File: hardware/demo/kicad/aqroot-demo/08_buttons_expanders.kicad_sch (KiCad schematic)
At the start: 30 parts, among them SW2 A_SELECT, SW3 UP, SW4 DOWN, SW5 LEFT, SW6 RIGHT, SW7 B_BACK, U2 PCAL9535APW, U3 PCAL9535APW

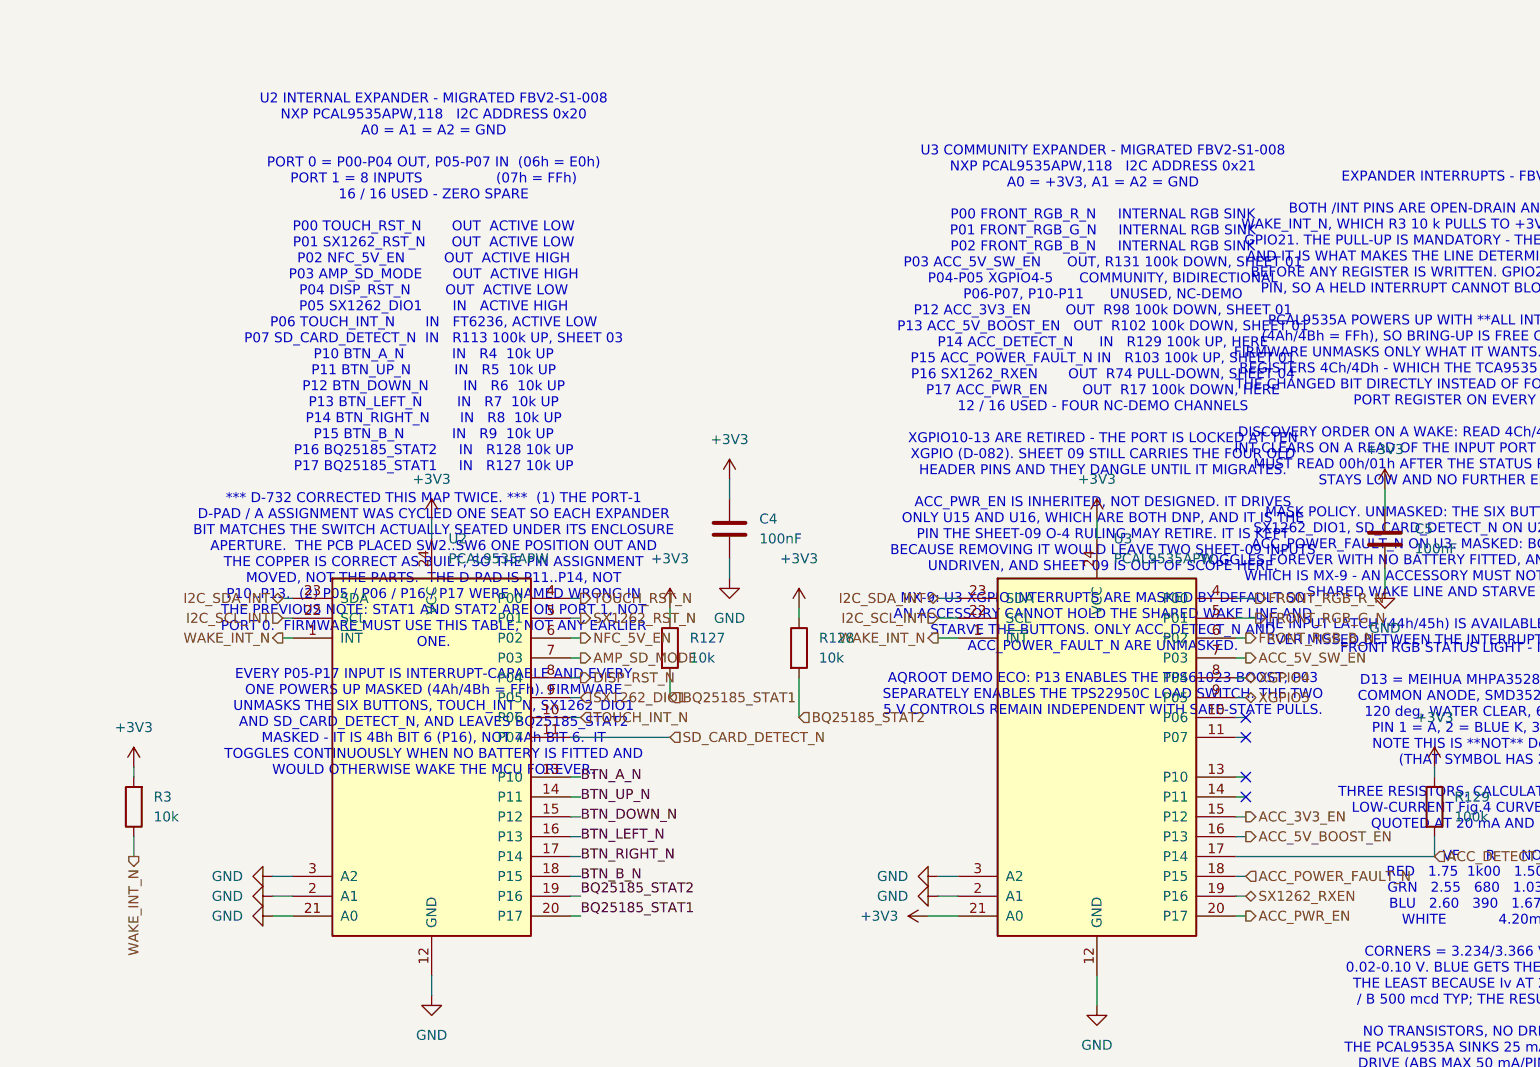
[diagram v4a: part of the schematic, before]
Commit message: demo: D-733 -- /ACC_PWR_EN is ROUTED and the community port's I2C buffer has its enable. 4 -> 3 retained open edges. What was holding it was /BQ25185_STAT1's 115.638 mm, 45-object western loop, which owns the only corridor from U16 into the U2-U3 pair; D-728 and D-731 both measured that ripping it closes ACC_PWR_EN and both stopped because STAT1 could not re-lay. D-732's lever opens it: an expander pin is a free variable, and STAT1's own surviving copper already passes 1.175 mm from U3.20 -- so STAT1 takes U3.20, ACC_PWR_EN takes the U2.20 that releases, and the loop is deleted. Both expanders are PCAL9535APW on the same internal bus sharing WAKE_INT_N, so the swap is behaviourally neutral; U2 P17 becomes that port's only output (07h FFh->7Fh) and R17's 100k keeps the safe state. STAT1's tail is a 1.025 mm hand lay that goes north first because U3's 1.475 mm lands make the straight 45-degree continuation pass 0.066 mm from U3.21. ACC_PWR_EN routes U16.1->U2.20 in 54.57 mm / 4 barrels, and only at 25 um: the 50 um rung is 0.47 mm shorter and carries a copper_sliver. Gate all clauses TRUE, verify_promotion PASS, DRC {lib_footprint_issues:199} only, parity 246/0 errors, 14/14 contracts PASS, protected_copper IDENTICAL.
Co-Authored-By: Claude Opus 5 <noreply@anthropic.com>
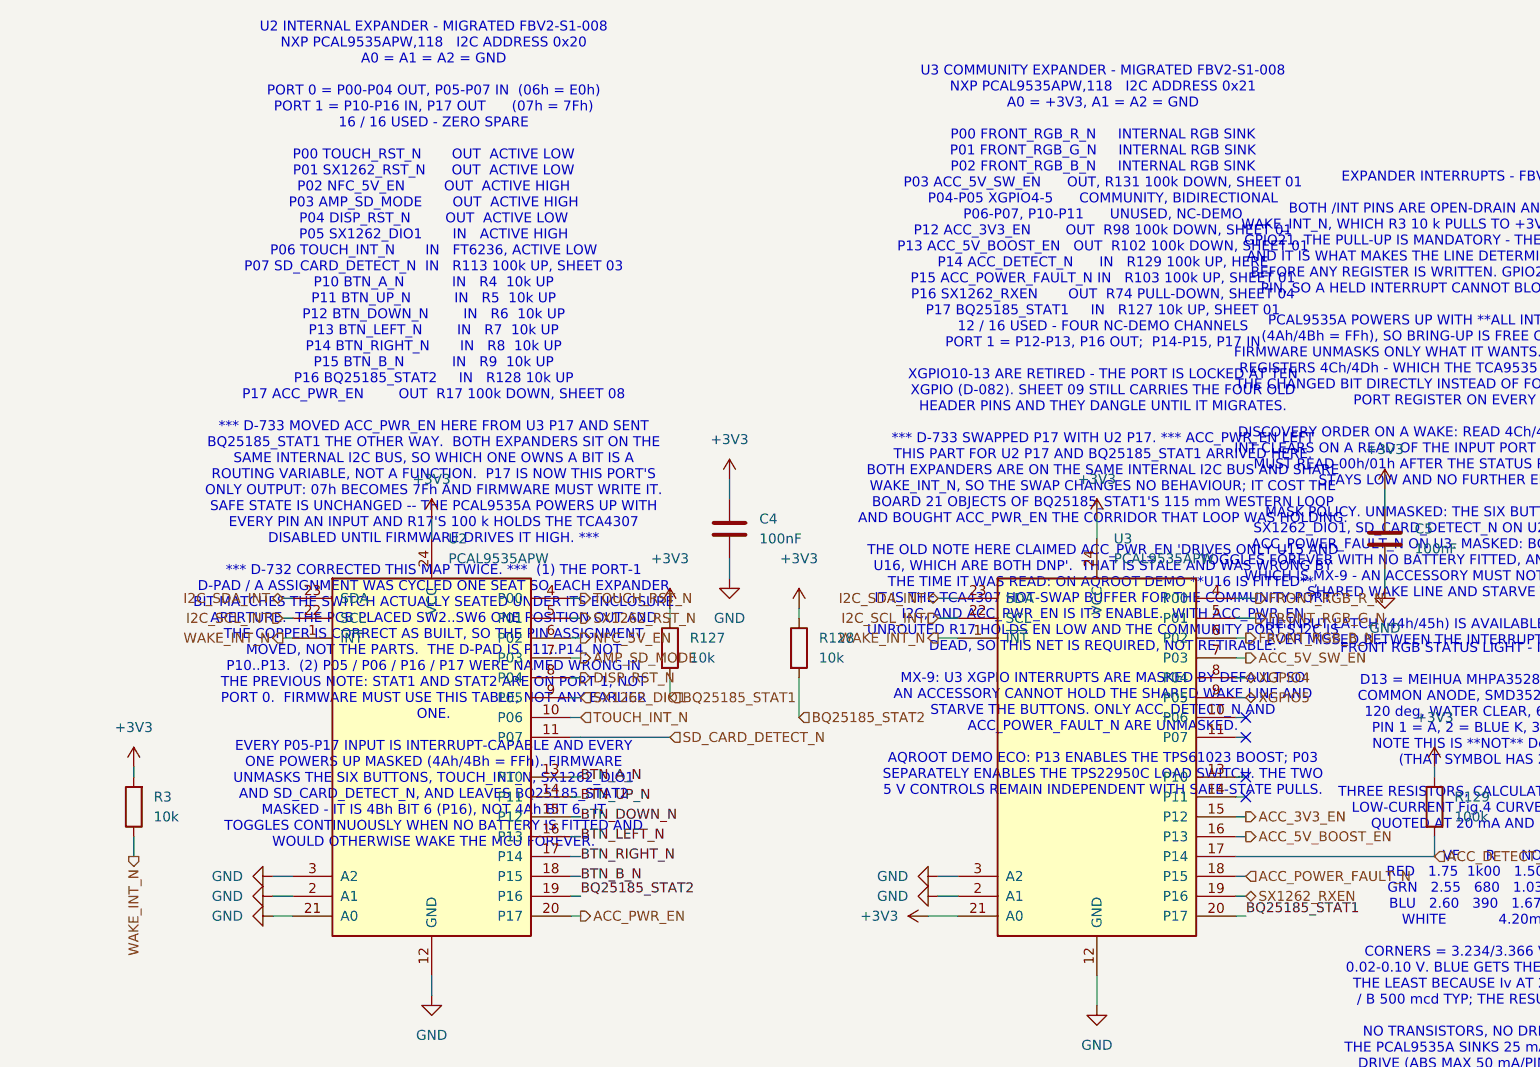
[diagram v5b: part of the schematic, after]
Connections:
- net ACC_PWR_EN: now also U2.20 (P17); no longer U3.20 (P17)
- net BQ25185_STAT1: now also U3.20 (P17); no longer U2.20 (P17)
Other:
- note added: "U2 INTERNAL EXPANDER - MIGRATED FBV2-S1-008 NXP PCAL9535APW,118 I2C ADDRESS 0x20 A0 = A1 = A2 = GND PORT 0 = P00-P04 OUT, P05-P07 IN (06h = E0h) PORT 1 = P10-P16 IN, P17 OUT (07h = 7Fh) 16 / 16 USED - ZERO SPARE P00 TOUCH_RST_N OUT ACTIVE LOW P01 SX1262_RST_N OUT ACTIVE LOW P02 NFC_5V_EN OUT ACTIVE HIGH P03 AMP_SD_MODE OUT ACTIVE HIGH P04 DISP_RST_N OUT ACTIVE LOW P05 SX1262_DIO1 IN ACTIVE HIGH P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"
- note removed: "U2 INTERNAL EXPANDER - MIGRATED FBV2-S1-008 NXP PCAL9535APW,118 I2C ADDRESS 0x20 A0 = A1 = A2 = GND PORT 0 = P00-P04 OUT, P05-P07 IN (06h = E0h) PORT 1 = 8 INPUTS (07h = FFh) 16 / 16 USED - ZERO SPARE P00 TOUCH_RST_N OUT ACTIVE LOW P01 SX1262_RST_N OUT ACTIVE LOW P02 NFC_5V_EN OUT ACTIVE HIGH P03 AMP_SD_MODE OUT ACTIVE HIGH P04 DISP_RST_N OUT ACTIVE LOW P05 SX1262_DIO1 IN ACTIVE HIGH P06 TOUCH_IN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"
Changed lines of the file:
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@@
 		(at 186.69 72.39)
 	)
-	(hierarchical_label "ACC_PWR_EN"
-		(shape output)
+	(label "BQ25185_STAT1"
 		(at 186.69 95.25 0)
 		(effects
@@
 				(size 1.27 1.27)
 			)
-			(justify left)
+			(justify left bottom)
 		)
 	)
@@
 		)
 	)
-	(label "BQ25185_STAT1"
+	(hierarchical_label "ACC_PWR_EN"
+		(shape output)
 		(at 101.6 95.25 0)
 		(effects
@@
 				(size 1.27 1.27)
 			)
-			(justify left bottom)
+			(justify left)
 		)
 	)
@@
 		)
 	)
-	(text "U2 INTERNAL EXPANDER - MIGRATED FBV2-S1-008\nNXP PCAL9535APW,118   I2C ADDRESS 0x20\nA0 = A1 = A2 = GND\n\nPORT 0 = P00-P04 OUT, P05-P07 IN  (06h = E0h)\nPORT 1 = 8 INPUTS                 (07h = FFh)\n16 / 16 USED - ZERO SPARE\n\nP00 TOUCH_RST_N       OUT  ACTIVE LOW\nP01 SX1262_RST_N      OUT  ACTIVE LOW\nP02 NFC_5V_EN         OUT  ACTIVE HIGH\nP03 AMP_SD_MODE       OUT  ACTIVE HIGH\nP04 DISP_RST_N        OUT  ACTIVE LOW\nP05 SX1262_DIO1       IN   ACTIVE HIGH\nP06 TOUCH_INT_N       IN   FT6236, ACTIVE LOW\nP07 SD_CARD_DETECT_N  IN   R113 100k UP, SHEET 03\nP10 BTN_A_N           IN   R4  10k UP\nP11 BTN_UP_N          IN   R5  10k UP\nP12 BTN_DOWN_N        IN   R6  10k UP\nP13 BTN_LEFT_N        IN   R7  10k UP\nP14 BTN_RIGHT_N       IN   R8  10k UP\nP15 BTN_B_N           IN   R9  10k UP\nP16 BQ25185_STAT2     IN   R128 10k UP\nP17 BQ25185_STAT1     IN   R127 10k UP\n\n*** D-732 CORRECTED THIS MAP TWICE. ***  (1) THE PORT-1\nD-PAD / A ASSIGNMENT WAS CYCLED ONE SEAT SO EACH EXPANDER\nBIT MATCHES THE SWITCH ACTUALLY SEATED UNDER ITS ENCLOSURE\nAPERTURE.  THE PCB PLACED SW2..SW6 ONE POSITION OUT AND\nTHE COPPER IS CORRECT AS BUILT, SO THE PIN ASSIGNMENT\nMOVED, NOT THE PARTS.  THE D-PAD IS P11..P14, NOT\nP10..P13.  (2) P05 / P06 / P16 / P17 WERE NAMED WRONG IN\nTHE PREVIOUS NOTE: STAT1 AND STAT2 ARE ON PORT 1, NOT\nPORT 0.  FIRMWARE MUST USE THIS TABLE, NOT ANY EARLIER\nONE.\n\nEVERY P05-P17 INPUT IS INTERRUPT-CAPABLE AND EVERY\nONE POWERS UP MASKED (4Ah/4Bh = FFh). FIRMWARE\nUNMASKS THE SIX BUTTONS, TOUCH_INT_N, SX1262_DIO1\nAND SD_CARD_DETECT_N, AND LEAVES BQ25185_STAT2\nMASKED - IT IS 4Bh BIT 6 (P16), NOT 4Ah BIT 6.  IT\nTOGGLES CONTINUOUSLY WHEN NO BATTERY IS FITTED AND\nWOULD OTHERWISE WAKE THE MCU FOREVER."
+	(text "U2 INTERNAL EXPANDER - MIGRATED FBV2-S1-008\nNXP PCAL9535APW,118   I2C ADDRESS 0x20\nA0 = A1 = A2 = GND\n\nPORT 0 = P00-P04 OUT, P05-P07 IN  (06h = E0h)\nPORT 1 = P10-P16 IN, P17 OUT      (07h = 7Fh)\n16 / 16 USED - ZERO SPARE\n\nP00 TOUCH_RST_N       OUT  ACTIVE LOW\nP01 SX1262_RST_N      OUT  ACTIVE LOW\nP02 NFC_5V_EN         OUT  ACTIVE HIGH\nP03 AMP_SD_MODE       OUT  ACTIVE HIGH\nP04 DISP_RST_N        OUT  ACTIVE LOW\nP05 SX1262_DIO1       IN   ACTIVE HIGH\nP06 TOUCH_INT_N       IN   FT6236, ACTIVE LOW\nP07 SD_CARD_DETECT_N  IN   R113 100k UP, SHEET 03\nP10 BTN_A_N           IN   R4  10k UP\nP11 BTN_UP_N          IN   R5  10k UP\nP12 BTN_DOWN_N        IN   R6  10k UP\nP13 BTN_LEFT_N        IN   R7  10k UP\nP14 BTN_RIGHT_N       IN   R8  10k UP\nP15 BTN_B_N           IN   R9  10k UP\nP16 BQ25185_STAT2     IN   R128 10k UP\nP17 ACC_PWR_EN        OUT  R17 100k DOWN, SHEET 08\n\n*** D-733 MOVED ACC_PWR_EN HERE FROM U3 P17 AND SENT\nBQ25185_STAT1 THE OTHER WAY.  BOTH EXPANDERS SIT ON THE\nSAME INTERNAL I2C BUS, SO WHICH ONE OWNS A BIT IS A\nROUTING VARIABLE, NOT A FUNCTION.  P17 IS NOW THIS PORT'S\nONLY OUTPUT: 07h BECOMES 7Fh AND FIRMWARE MUST WRITE IT.\nSAFE STATE IS UNCHANGED -- THE PCAL9535A POWERS UP WITH\nEVERY PIN AN INPUT AND R17'S 100 k HOLDS THE TCA4307\nDISABLED UNTIL FIRMWARE DRIVES IT HIGH. ***\n\n*** D-732 CORRECTED THIS MAP TWICE. ***  (1) THE PORT-1\nD-PAD / A ASSIGNMENT WAS CYCLED ONE SEAT SO EACH EXPANDER\nBIT MATCHES THE SWITCH ACTUALLY SEATED UNDER ITS ENCLOSURE\nAPERTURE.  THE PCB PLACED SW2..SW6 ONE POSITION OUT AND\nTHE COPPER IS CORRECT AS BUILT, SO THE PIN ASSIGNMENT\nMOVED, NOT THE PARTS.  THE D-PAD IS P11..P14, NOT\nP10..P13.  (2) P05 / P06 / P16 / P17 WERE NAMED WRONG IN\nTHE PREVIOUS NOTE: STAT1 AND STAT2 ARE ON PORT 1, NOT\nPORT 0.  FIRMWARE MUST USE THIS TABLE, NOT ANY EARLIER\nONE.\n\nEVERY P05-P17 INPUT IS INTERRUPT-CAPABLE AND EVERY\nONE POWERS UP MASKED (4Ah/4Bh = FFh). FIRMWARE\nUNMASKS THE SIX BUTTONS, TOUCH_INT_N, SX1262_DIO1\nAND SD_CARD_DETECT_N, AND LEAVES BQ25185_STAT2\nMASKED - IT IS 4Bh BIT 6 (P16), NOT 4Ah BIT 6.  IT\nTOGGLES CONTINUOUSLY WHEN NO BATTERY IS FITTED AND\nWOULD OTHERWISE WAKE THE MCU FOREVER."
 		(exclude_from_sim no)
 		(at 82.804 33.782 0)
@@
 		)
 	)
-	(text "U3 COMMUNITY EXPANDER - MIGRATED FBV2-S1-008\nNXP PCAL9535APW,118   I2C ADDRESS 0x21\nA0 = +3V3, A1 = A2 = GND\n\nP00 FRONT_RGB_R_N     INTERNAL RGB SINK\nP01 FRONT_RGB_G_N     INTERNAL RGB SINK\nP02 FRONT_RGB_B_N     INTERNAL RGB SINK\nP03 ACC_5V_SW_EN      OUT, R131 100k DOWN, SHEET 01\nP04-P05 XGPIO4-5      COMMUNITY, BIDIRECTIONAL\nP06-P07, P10-P11      UNUSED, NC-DEMO\nP12 ACC_3V3_EN        OUT  R98 100k DOWN, SHEET 01\nP13 ACC_5V_BOOST_EN   OUT  R102 100k DOWN, SHEET 01\nP14 ACC_DETECT_N      IN   R129 100k UP, HERE\nP15 ACC_POWER_FAULT_N IN   R103 100k UP, SHEET 01\nP16 SX1262_RXEN       OUT  R74 PULL-DOWN, SHEET 04\nP17 ACC_PWR_EN        OUT  R17 100k DOWN, HERE\n12 / 16 USED - FOUR NC-DEMO CHANNELS\n\nXGPIO10-13 ARE RETIRED - THE PORT IS LOCKED AT TEN\nXGPIO (D-082). SHEET 09 STILL CARRIES THE FOUR OLD\nHEADER PINS AND THEY DANGLE UNTIL IT MIGRATES.\n\nACC_PWR_EN IS INHERITED, NOT DESIGNED. IT DRIVES\nONLY U15 AND U16, WHICH ARE BOTH DNP, AND IT IS THE\nPIN THE SHEET-09 O-4 RULING MAY RETIRE. IT IS KEPT\nBECAUSE REMOVING IT WOULD LEAVE TWO SHEET-09 INPUTS\nUNDRIVEN, AND SHEET 09 IS OUT OF SCOPE HERE.\n\nMX-9: U3 XGPIO INTERRUPTS ARE MASKED BY DEFAULT SO\nAN ACCESSORY CANNOT HOLD THE SHARED WAKE LINE AND\nSTARVE THE BUTTONS. ONLY ACC_DETECT_N AND\nACC_POWER_FAULT_N ARE UNMASKED.\n\nAQROOT DEMO ECO: P13 ENABLES THE TPS61023 BOOST; P03\nSEPARATELY ENABLES THE TPS22950C LOAD SWITCH. THE TWO\n5 V CONTROLS REMAIN INDEPENDENT WITH SAFE-STATE PULLS."
+	(text "U3 COMMUNITY EXPANDER - MIGRATED FBV2-S1-008\nNXP PCAL9535APW,118   I2C ADDRESS 0x21\nA0 = +3V3, A1 = A2 = GND\n\nP00 FRONT_RGB_R_N     INTERNAL RGB SINK\nP01 FRONT_RGB_G_N     INTERNAL RGB SINK\nP02 FRONT_RGB_B_N     INTERNAL RGB SINK\nP03 ACC_5V_SW_EN      OUT, R131 100k DOWN, SHEET 01\nP04-P05 XGPIO4-5      COMMUNITY, BIDIRECTIONAL\nP06-P07, P10-P11      UNUSED, NC-DEMO\nP12 ACC_3V3_EN        OUT  R98 100k DOWN, SHEET 01\nP13 ACC_5V_BOOST_EN   OUT  R102 100k DOWN, SHEET 01\nP14 ACC_DETECT_N      IN   R129 100k UP, HERE\nP15 ACC_POWER_FAULT_N IN   R103 100k UP, SHEET 01\nP16 SX1262_RXEN       OUT  R74 PULL-DOWN, SHEET 04\nP17 BQ25185_STAT1     IN   R127 10k UP, SHEET 01\n12 / 16 USED - FOUR NC-DEMO CHANNELS\nPORT 1 = P12-P13, P16 OUT;  P14-P15, P17 IN\n\nXGPIO10-13 ARE RETIRED - THE PORT IS LOCKED AT TEN\nXGPIO (D-082). SHEET 09 STILL CARRIES THE FOUR OLD\nHEADER PINS AND THEY DANGLE UNTIL IT MIGRATES.\n\n*** D-733 SWAPPED P17 WITH U2 P17. *** ACC_PWR_EN LEFT\nTHIS PART FOR U2 P17 AND BQ25185_STAT1 ARRIVED HERE.\nBOTH EXPANDERS ARE ON THE SAME INTERNAL I2C BUS AND SHARE\nWAKE_INT_N, SO THE SWAP CHANGES NO BEHAVIOUR; IT COST THE\nBOARD 21 OBJECTS OF BQ25185_STAT1'S 115 mm WESTERN LOOP\nAND BOUGHT ACC_PWR_EN THE CORRIDOR THAT LOOP WAS HOLDING.\n\nTHE OLD NOTE HERE CLAIMED ACC_PWR_EN 'DRIVES ONLY U15 AND\nU16, WHICH ARE BOTH DNP'.  THAT IS STALE AND WAS WRONG BY\nTHE TIME IT WAS READ: ON AQROOT DEMO **U16 IS FITTED**,\nIT IS THE TCA4307 HOT-SWAP BUFFER FOR THE COMMUNITY-PORT\nI2C, AND ACC_PWR_EN IS ITS ENABLE.  WITH ACC_PWR_EN\nUNROUTED R17 HOLDS EN LOW AND THE COMMUNITY PORT'S I2C IS\nDEAD, SO THIS NET IS REQUIRED, NOT RETIRABLE.\n\nMX-9: U3 XGPIO INTERRUPTS ARE MASKED BY DEFAULT SO\nAN ACCESSORY CANNOT HOLD THE SHARED WAKE LINE AND\nSTARVE THE BUTTONS. ONLY ACC_DETECT_N AND\nACC_POWER_FAULT_N ARE UNMASKED.\n\nAQROOT DEMO ECO: P13 ENABLES THE TPS61023 BOOST; P03\nSEPARATELY ENABLES THE TPS22950C LOAD SWITCH. THE TWO\n5 V CONTROLS REMAIN INDEPENDENT WITH SAFE-STATE PULLS."
 		(exclude_from_sim no)
 		(at 168.402 33.274 0)
